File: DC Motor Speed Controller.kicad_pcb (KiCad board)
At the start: 2 copper layers, 15 parts, among them J1 Screw_Terminal_01x02, J2 Screw_Terminal_01x02, Q1 TIP122, U1 NE555P

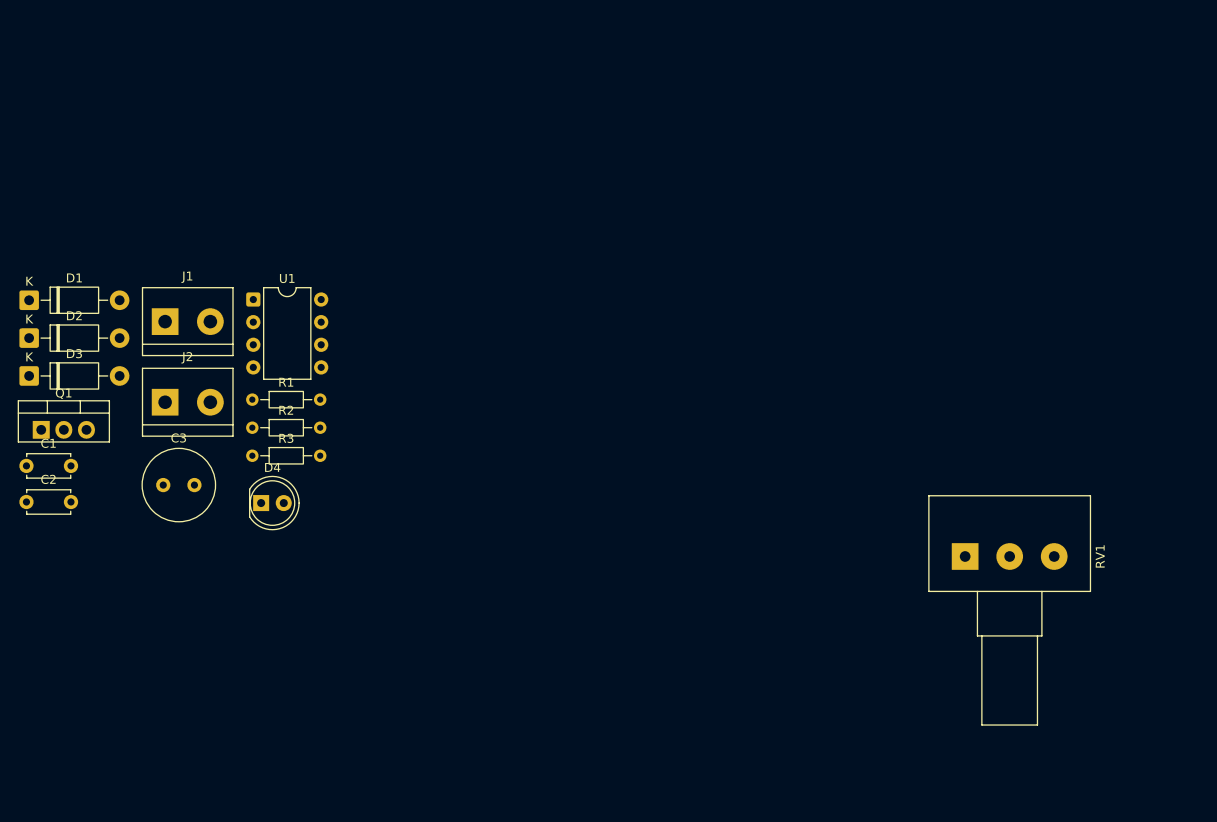
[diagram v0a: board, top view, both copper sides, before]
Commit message: Added Footprints to PCB Editor
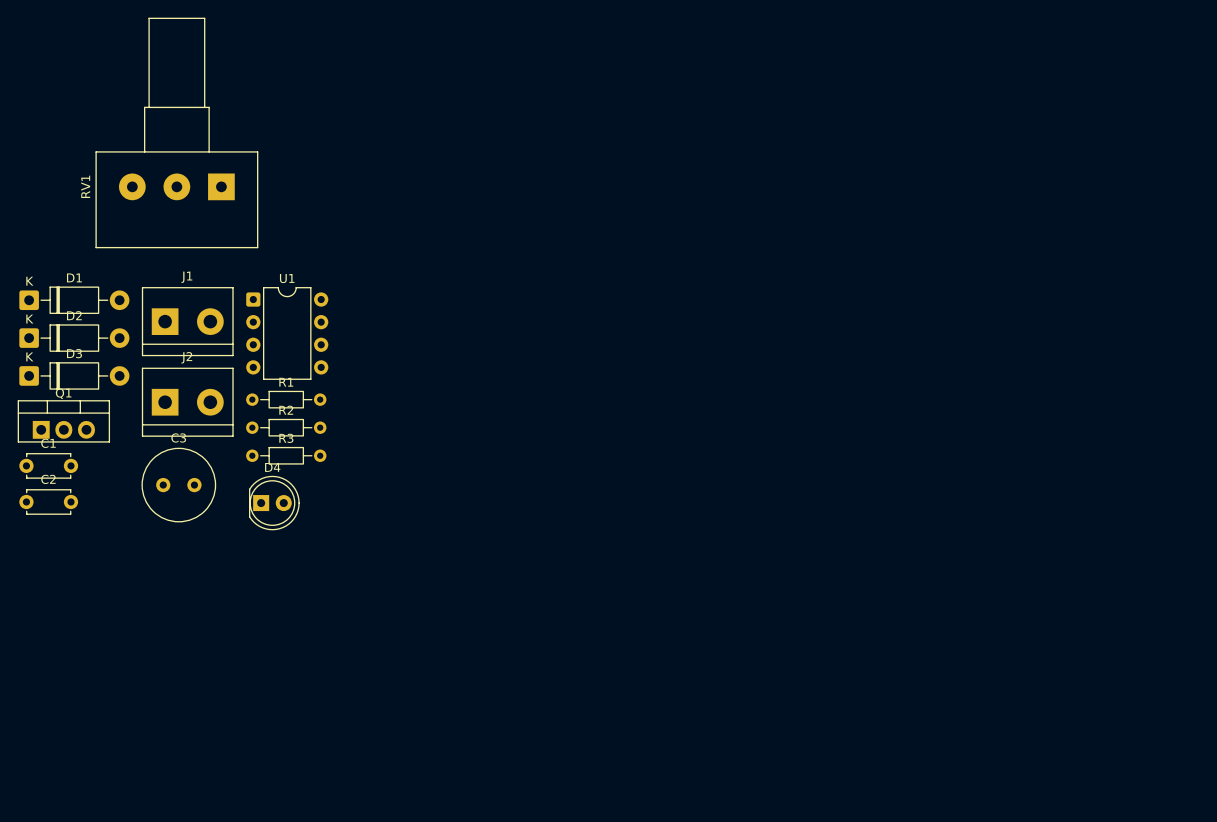
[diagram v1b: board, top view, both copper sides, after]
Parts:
- moved RV1 93.2 mm to (75.2, 42.2), turned to -90 degrees
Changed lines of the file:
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@@
 	(footprint "Potentiometer_THT:Potentiometer_Alps_RK163_Single_Horizontal"
 		(layer "F.Cu")
-		(at 158.75 83.75 90)
+		(at 75.25 42.25 -90)
 		(descr "1110U1Q 1110TNP 1110U2A 1110U0Q Potentiometer, horizontal, Alps RK163 Single, https://tech.alpsalpine.com/prod/e/pdf/potentiometer/rotarypotentiometers/rk16/rk16.pdf")
 		(tags "Potentiometer horizontal Alps RK163 Single")
@@
 		)
 		(property "Datasheet" ""
-			(at 0 0 90)
+			(at 0 0 270)
 			(unlocked yes)
 			(layer "F.Fab")
@@
 		)
 		(property "Description" "Potentiometer"
-			(at 0 0 90)
+			(at 0 0 270)
 			(unlocked yes)
 			(layer "F.Fab")
@@
 		(attr through_hole)
 		(fp_line
+			(start -3.92 14.07)
+			(end -3.92 -4.07)
+			(stroke
+				(width 0.12)
+				(type solid)
+			)
+			(layer "F.SilkS")
+		)
+		(fp_line
+			(start 6.82 14.07)
+			(end -3.92 14.07)
+			(stroke
+				(width 0.12)
+				(type solid)
+			)
+			(layer "F.SilkS")
+		)
+		(fp_line
+			(start 6.82 14.07)
+			(end 6.82 -4.07)
+			(stroke
+				(width 0.12)
+				(type solid)
+			)
+			(layer "F.SilkS")
+		)
+		(fp_line
+			(start -8.92 8.62)
+			(end -8.92 1.38)
+			(stroke
+				(width 0.12)
+				(type solid)
+			)
+			(layer "F.SilkS")
+		)
+		(fp_line
+			(start -3.92 8.62)
+			(end -8.92 8.62)
+			(stroke
+				(width 0.12)
+				(type solid)
+			)
+			(layer "F.SilkS")
+		)
+		(fp_line
+			(start -18.92 8.12)
+			(end -18.92 1.88)
+			(stroke
+				(width 0.12)
+				(type solid)
+			)
+			(layer "F.SilkS")
+		)
+		(fp_line
+			(start -8.92 8.12)
+			(end -18.92 8.12)
+			(stroke
+				(width 0.12)
+				(type solid)
+			)
+			(layer "F.SilkS")
+		)
+		(fp_line
+			(start -8.92 1.88)
+			(end -18.92 1.88)
+			(stroke
+				(width 0.12)
+				(type solid)
+			)
+			(layer "F.SilkS")
+		)
+		(fp_line
+			(start -3.92 1.38)
+			(end -8.92 1.38)
+			(stroke
+				(width 0.12)
+				(type solid)
+			)
+			(layer "F.SilkS")
+		)
+		(fp_line
 			(start 6.82 -4.07)
 			(end -3.92 -4.07)
@@
 		)
 		(fp_line
-			(start -3.92 1.38)
-			(end -8.92 1.38)
-			(stroke
-				(width 0.12)
-				(type solid)
-			)
-			(layer "F.SilkS")
-		)
-		(fp_line
-			(start -8.92 1.88)
-			(end -18.92 1.88)
-			(stroke
-				(width 0.12)
-				(type solid)
-			)
-			(layer "F.SilkS")
-		)
-		(fp_line
-			(start -8.92 8.12)
-			(end -18.92 8.12)
-			(stroke
-				(width 0.12)
-				(type solid)
-			)
-			(layer "F.SilkS")
-		)
-		(fp_line
-			(start -18.92 8.12)
-			(end -18.92 1.88)
-			(stroke
-				(width 0.12)
-				(type solid)
-			)
-			(layer "F.SilkS")
-		)
-		(fp_line
-			(start -3.92 8.62)
-			(end -8.92 8.62)
-			(stroke
-				(width 0.12)
-				(type solid)
-			)
-			(layer "F.SilkS")
-		)
-		(fp_line
-			(start -8.92 8.62)
-			(end -8.92 1.38)
-			(stroke
-				(width 0.12)
-				(type solid)
-			)
-			(layer "F.SilkS")
-		)
-		(fp_line
-			(start 6.82 14.07)
-			(end 6.82 -4.07)
-			(stroke
-				(width 0.12)
-				(type solid)
-			)
-			(layer "F.SilkS")
-		)
-		(fp_line
-			(start 6.82 14.07)
-			(end -3.92 14.07)
-			(stroke
-				(width 0.12)
-				(type solid)
-			)
-			(layer "F.SilkS")
-		)
-		(fp_line
-			(start -3.92 14.07)
-			(end -3.92 -4.07)
-			(stroke
-				(width 0.12)
-				(type solid)
-			)
-			(layer "F.SilkS")
+			(start -19.05 14.2)
+			(end 6.95 14.2)
+			(stroke
+				(width 0.05)
+				(type solid)
+			)
+			(layer "F.CrtYd")
+		)
+		(fp_line
+			(start 6.95 14.2)
+			(end 6.95 -4.2)
+			(stroke
+				(width 0.05)
+				(type solid)
+			)
+			(layer "F.CrtYd")
+		)
+		(fp_line
+			(start -19.05 -4.2)
+			(end -19.05 14.2)
+			(stroke
+				(width 0.05)
+				(type solid)
+			)
+			(layer "F.CrtYd")
 		)
 		(fp_line
@@
 		)
 		(fp_line
-			(start -19.05 -4.2)
-			(end -19.05 14.2)
-			(stroke
-				(width 0.05)
-				(type solid)
-			)
-			(layer "F.CrtYd")
-		)
-		(fp_line
-			(start 6.95 14.2)
-			(end 6.95 -4.2)
-			(stroke
-				(width 0.05)
-				(type solid)
-			)
-			(layer "F.CrtYd")
-		)
-		(fp_line
-			(start -19.05 14.2)
-			(end 6.95 14.2)
-			(stroke
-				(width 0.05)
-				(type solid)
-			)
-			(layer "F.CrtYd")
+			(start -3.8 13.95)
+			(end 6.7 13.95)
+			(stroke
+				(width 0.1)
+				(type solid)
+			)
+			(layer "F.Fab")
+		)
+		(fp_line
+			(start 6.7 13.95)
+			(end 6.7 -3.95)
+			(stroke
+				(width 0.1)
+				(type solid)
+			)
+			(layer "F.Fab")
+		)
+		(fp_line
+			(start -8.8 8.5)
+			(end -3.8 8.5)
+			(stroke
+				(width 0.1)
+				(type solid)
+			)
+			(layer "F.Fab")
+		)
+		(fp_line
+			(start -18.8 8)
+			(end -8.8 8)
+			(stroke
+				(width 0.1)
+				(type solid)
+			)
+			(layer "F.Fab")
+		)
+		(fp_line
+			(start -18.8 2)
+			(end -18.8 8)
+			(stroke
+				(width 0.1)
+				(type solid)
+			)
+			(layer "F.Fab")
+		)
+		(fp_line
+			(start -8.8 2)
+			(end -18.8 2)
+			(stroke
+				(width 0.1)
+				(type solid)
+			)
+			(layer "F.Fab")
+		)
+		(fp_line
+			(start -8.8 1.5)
+			(end -8.8 8.5)
+			(stroke
+				(width 0.1)
+				(type solid)
+			)
+			(layer "F.Fab")
+		)
+		(fp_line
+			(start -3.8 1.5)
+			(end -8.8 1.5)
+			(stroke
+				(width 0.1)
+				(type solid)
+			)
+			(layer "F.Fab")
+		)
+		(fp_line
+			(start -3.8 -3.95)
+			(end -3.8 13.95)
+			(stroke
+				(width 0.1)
+				(type solid)
+			)
+			(layer "F.Fab")
 		)
 		(fp_line
@@
 			(layer "F.Fab")
 		)
-		(fp_line
-			(start -3.8 -3.95)
-			(end -3.8 13.95)
-			(stroke
-				(width 0.1)
-				(type solid)
-			)
-			(layer "F.Fab")
-		)
-		(fp_line
-			(start -3.8 1.5)
-			(end -8.8 1.5)
-			(stroke
-				(width 0.1)
-				(type solid)
-			)
-			(layer "F.Fab")
-		)
-		(fp_line
-			(start -8.8 1.5)
-			(end -8.8 8.5)
-			(stroke
-				(width 0.1)
-				(type solid)
-			)
-			(layer "F.Fab")
-		)
-		(fp_line
-			(start -8.8 2)
-			(end -18.8 2)
-			(stroke
-				(width 0.1)
-				(type solid)
-			)
-			(layer "F.Fab")
-		)
-		(fp_line
-			(start -18.8 2)
-			(end -18.8 8)
-			(stroke
-				(width 0.1)
-				(type solid)
-			)
-			(layer "F.Fab")
-		)
-		(fp_line
-			(start -18.8 8)
-			(end -8.8 8)
-			(stroke
-				(width 0.1)
-				(type solid)
-			)
-			(layer "F.Fab")
-		)
-		(fp_line
-			(start -8.8 8.5)
-			(end -3.8 8.5)
-			(stroke
-				(width 0.1)
-				(type solid)
-			)
-			(layer "F.Fab")
-		)
-		(fp_line
-			(start 6.7 13.95)
-			(end 6.7 -3.95)
-			(stroke
-				(width 0.1)
-				(type solid)
-			)
-			(layer "F.Fab")
-		)
-		(fp_line
-			(start -3.8 13.95)
-			(end 6.7 13.95)
-			(stroke
-				(width 0.1)
-				(type solid)
-			)
-			(layer "F.Fab")
-		)
 		(fp_text user "${REFERENCE}"
 			(at 1.45 4.999999 90)
@@
 		)
 		(pad "1" thru_hole rect
-			(at 0 0 270)
+			(at 0 0 90)
 			(size 3 3)
 			(drill 1.2)
@@
 		)
 		(pad "2" thru_hole circle
-			(at 0 5 270)
+			(at 0 5 90)
 			(size 3 3)
 			(drill 1.2)
@@
 		)
 		(pad "3" thru_hole circle
-			(at 0 10 270)
+			(at 0 10 90)
 			(size 3 3)
 			(drill 1.2)

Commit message: Placed the Footprints at Place
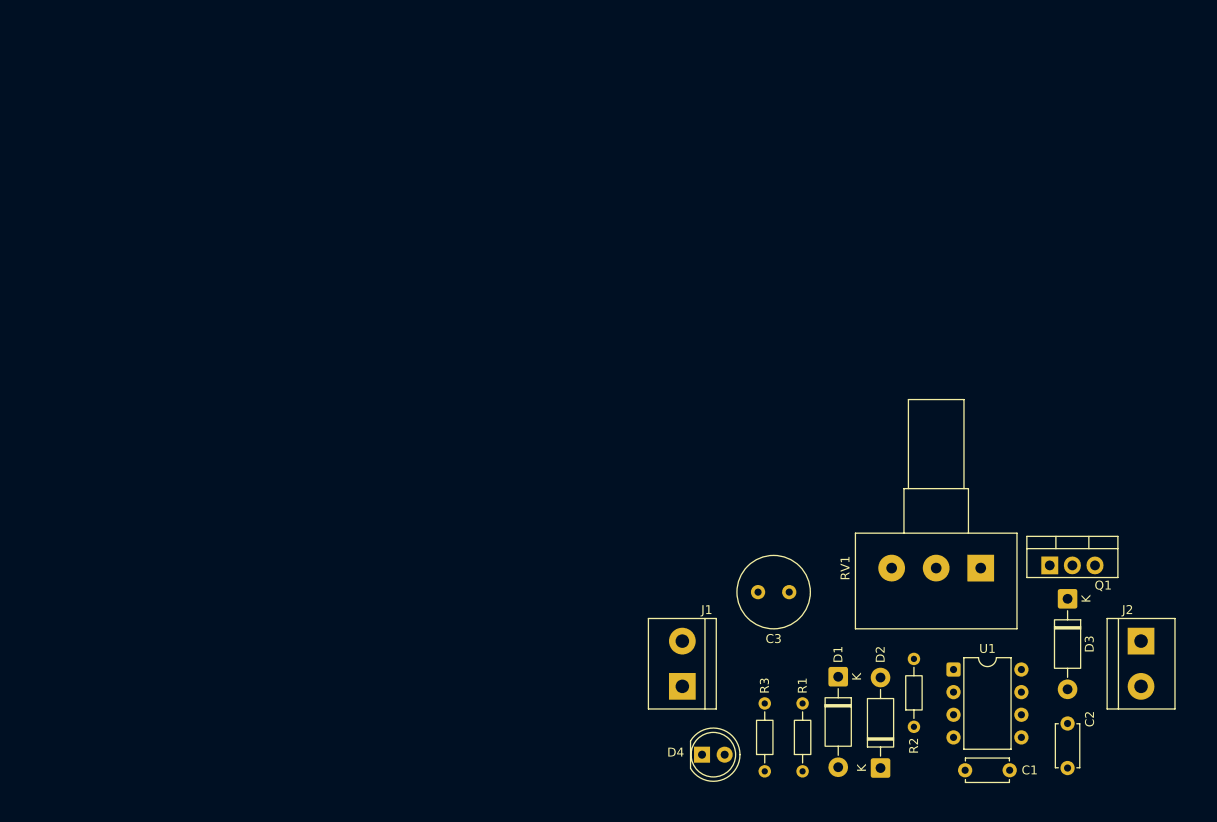
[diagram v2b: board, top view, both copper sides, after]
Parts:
- moved C2 119.5 mm to (170.2, 102.5), turned to -90 degrees
- moved D3 119.2 mm to (170.2, 88.5), turned to -90 degrees
- moved Q1 114.2 mm to (168.2, 84.8)
- moved J2 112.8 mm to (178.5, 93.2), turned to -90 degrees
- moved C1 110.8 mm to (158.8, 107.8)
- moved D2 107.1 mm to (149.2, 107.5), turned to 90 degrees
- moved D1 100.2 mm to (144.5, 97.2), turned to -90 degrees
- moved RV1 95.4 mm to (160.5, 85.0)
- moved U1 88.9 mm to (157.4, 96.4)
- moved R2 81.5 mm to (153.0, 102.9), turned to 90 degrees
- moved R1 74.6 mm to (140.5, 107.9), turned to 90 degrees
- moved J1 71.1 mm to (127.0, 98.3), turned to 90 degrees
- moved C3 67.9 mm to (135.5, 87.8)
- moved R3 67.6 mm to (136.2, 107.9), turned to 90 degrees
- moved D4 57.0 mm to (129.2, 106.0)

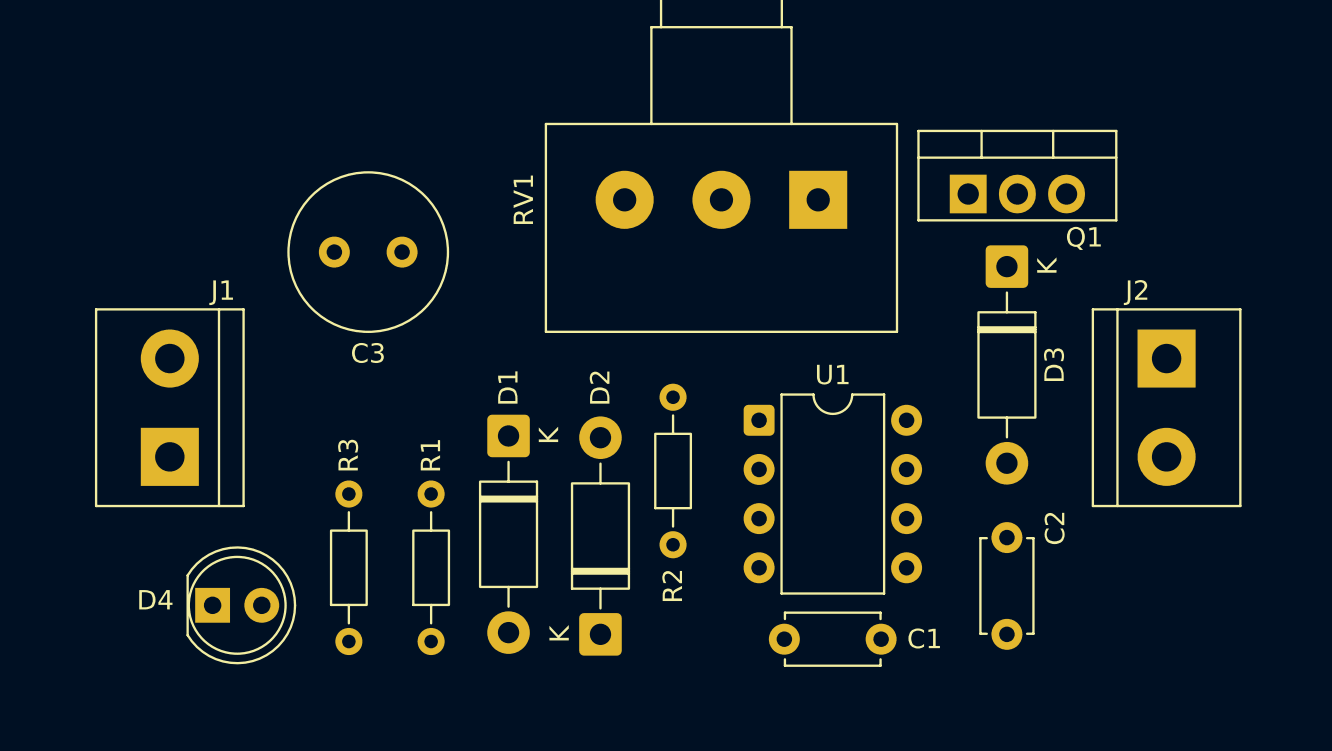
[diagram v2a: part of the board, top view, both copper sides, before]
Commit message: Added Edge Cuts to PCB
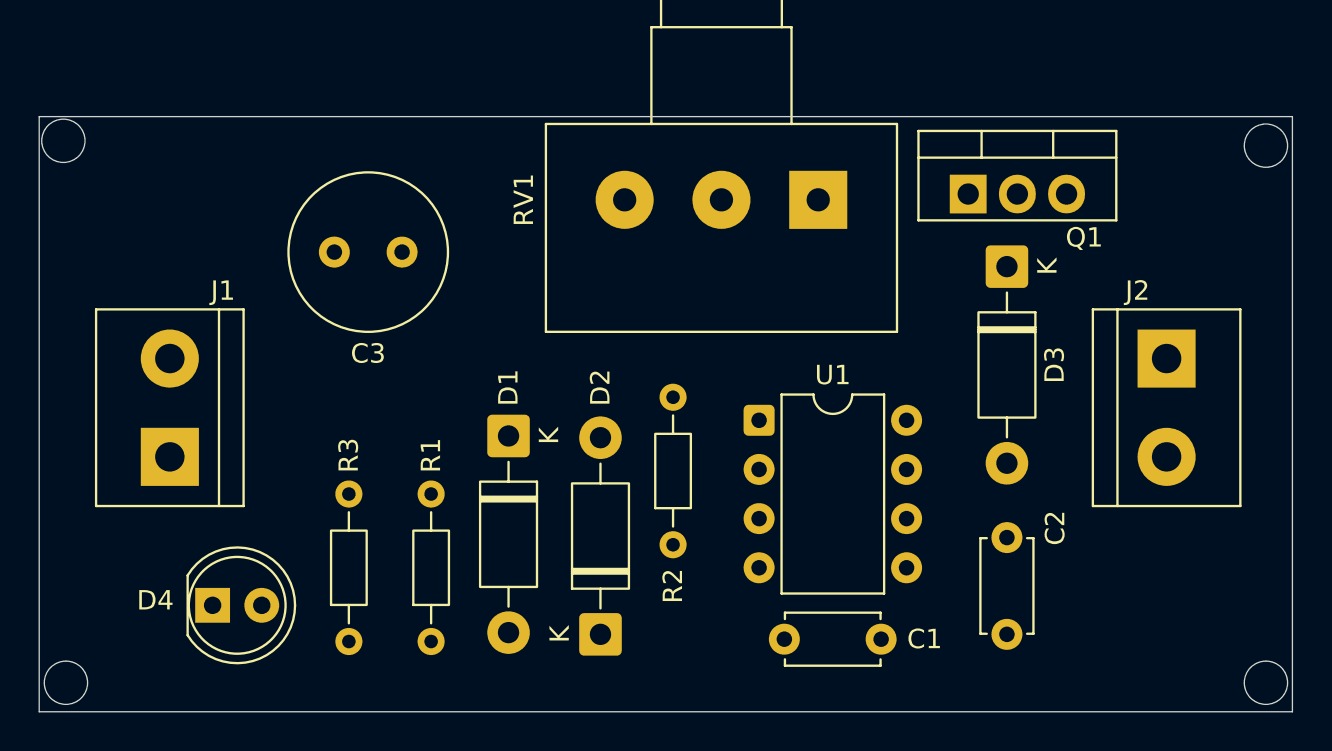
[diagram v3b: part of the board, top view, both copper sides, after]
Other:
- board outline added: 64.8 x 30.8 mm
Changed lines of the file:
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@@
 		)
+	)
+	(gr_circle
+		(center 183.631966 110)
+		(end 182.631966 109.5)
+		(stroke
+			(width 0.05)
+			(type default)
+		)
+		(fill no)
+		(layer "Edge.Cuts")
+	)
+	(gr_rect
+		(start 120.25 80.75)
+		(end 185 111.5)
+		(stroke
+			(width 0.05)
+			(type default)
+		)
+		(fill no)
+		(layer "Edge.Cuts")
+	)
+	(gr_circle
+		(center 121.631966 110)
+		(end 120.631966 109.5)
+		(stroke
+			(width 0.05)
+			(type default)
+		)
+		(fill no)
+		(layer "Edge.Cuts")
+	)
+	(gr_circle
+		(center 183.631966 82.25)
+		(end 182.631966 81.75)
+		(stroke
+			(width 0.05)
+			(type default)
+		)
+		(fill no)
+		(layer "Edge.Cuts")
+	)
+	(gr_circle
+		(center 121.5 82)
+		(end 120.5 81.5)
+		(stroke
+			(width 0.05)
+			(type default)
+		)
+		(fill no)
+		(layer "Edge.Cuts")
 	)
 	(embedded_fonts no)
